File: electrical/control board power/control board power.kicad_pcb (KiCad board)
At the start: 2 copper layers, 147.3 x 147.3 mm, 69 parts, among them J1 Conn_01x02, J10 48V_from_conversion, J17 Switch_B, J18 Switch_C, J19 Switch_D, J2 5V, J3 Barrel_Jack, J4 Switch_A, J5 Switch_Input, J6 Power_Connector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

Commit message: Found some parts
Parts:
- added C14: C_Small, Capacitor_SMD:C_0603_1608Metric_Pad1.05x0.95mm_HandSolder, F.Cu at (25.9, 53.9)
- added R11: 1m, footprints:FC4L64, F.Cu at (34.4, 53.4)
- added U4: INA240-INA240, Package_SO:TSSOP-8_4.4x3mm_P0.65mm, F.Cu at (28.2, 51.4)
- R16, R3: footprint Resistor_SMD:R_0603_1608Metric_Pad1.05x0.95mm_HandSolder -> Resistor_SMD:R_1206_3216Metric_Pad1.42x1.75mm_HandSolder
- moved J1 23.1 mm to (81.2, 141.5)
- moved D1 7.40 mm to (45.5, 76.5)
- moved D3 7.40 mm to (45.5, 82.5)
- moved D8 7.40 mm to (45.5, 79.5)
- moved R1 7.40 mm to (50.5, 76.5)
- moved R16 7.40 mm to (50.5, 79.5)
- moved R3 7.40 mm to (50.5, 82.5)
- moved D2 7.40 mm to (45.5, 73.4)
- moved R2 7.40 mm to (50.5, 73.4)
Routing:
- net +24V: track 60.8 -> 91.7 mm
- net +5V: track 242.7 -> 250.5 mm
- net +48V: track 307.1 -> 313.8 mm
- net +3V3: track 59.6 -> 66.2 mm
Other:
- board text added: "These need to move"

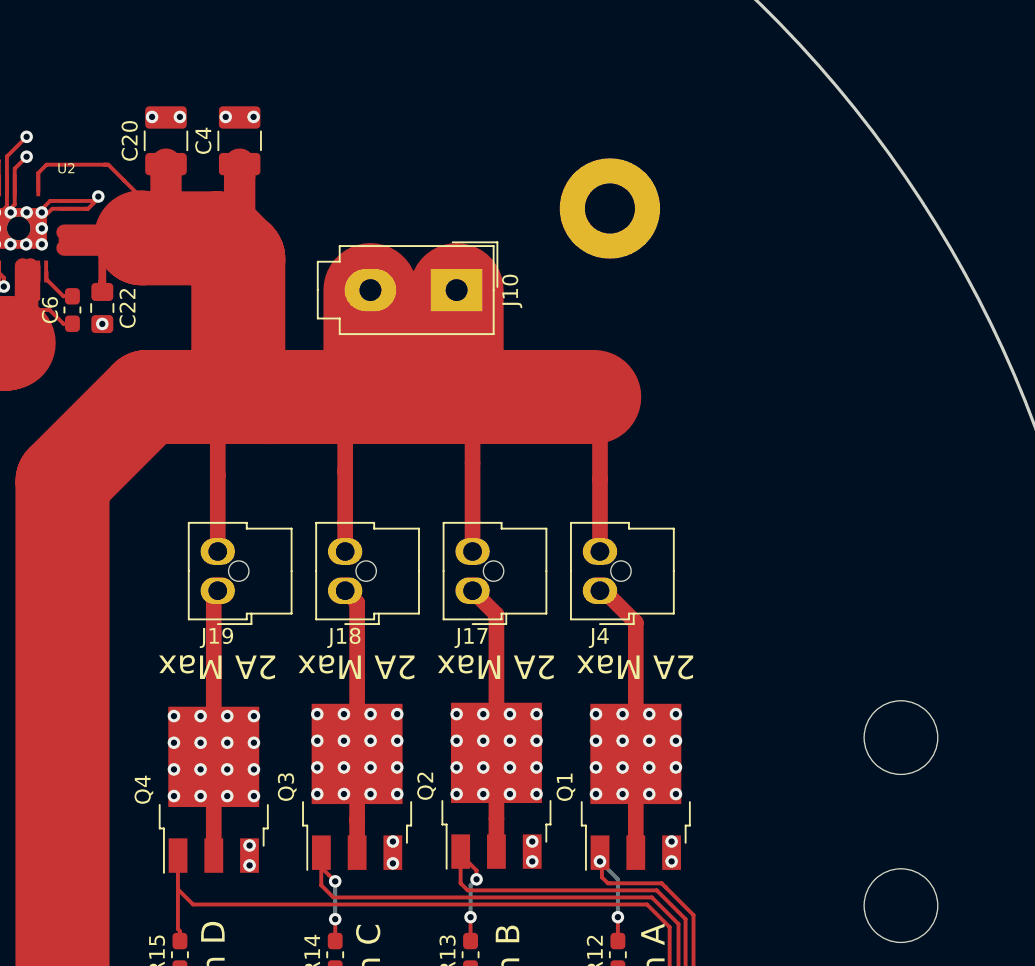
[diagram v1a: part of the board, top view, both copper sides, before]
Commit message: Making the low side switches beefier
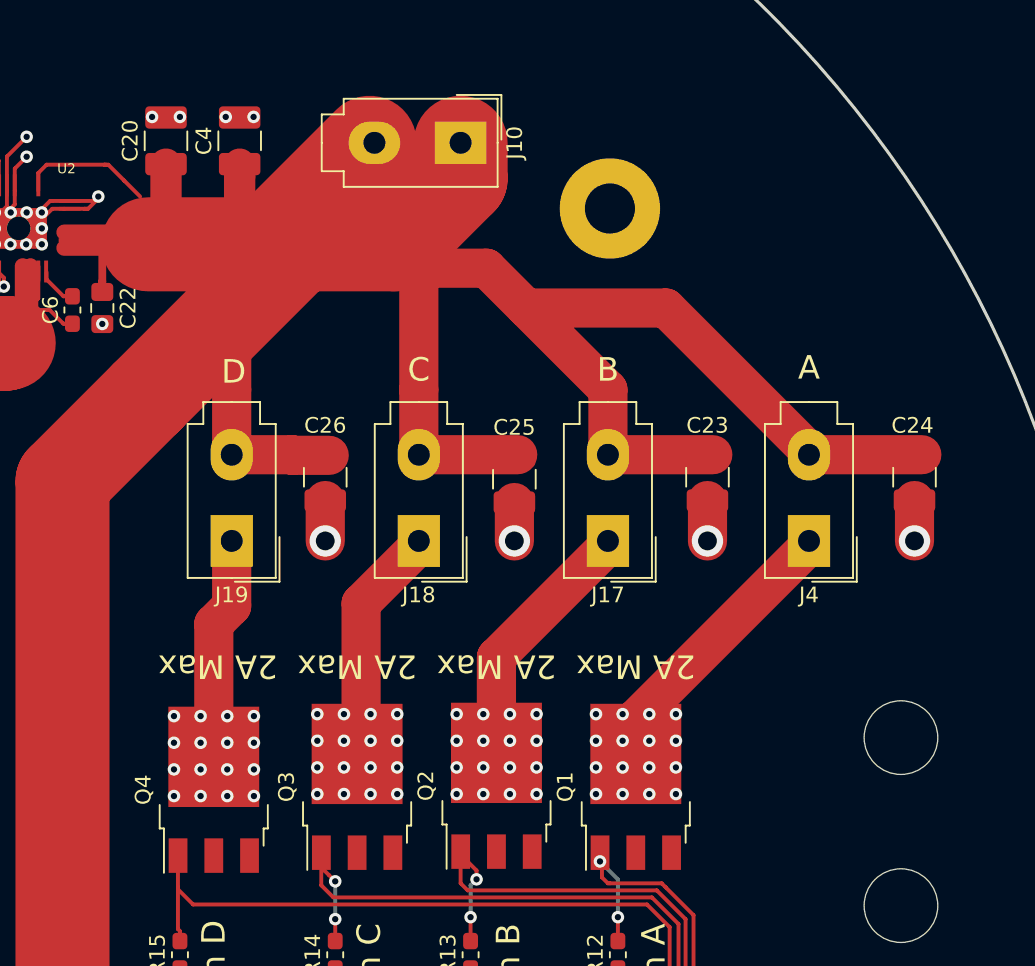
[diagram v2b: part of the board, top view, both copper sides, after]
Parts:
- added C23: 10uF, Capacitor_SMD:C_1210_3225Metric_Pad1.42x2.65mm_HandSolder, F.Cu at (149.7, 79.9)
- added C24: 10uF, Capacitor_SMD:C_1210_3225Metric_Pad1.42x2.65mm_HandSolder, F.Cu at (162.9, 79.9)
- added C25: 10uF, Capacitor_SMD:C_1210_3225Metric_Pad1.42x2.65mm_HandSolder, F.Cu at (137.4, 80.0)
- added C26: 10uF, Capacitor_SMD:C_1210_3225Metric_Pad1.42x2.65mm_HandSolder, F.Cu at (125.3, 79.9)
- J17, J18, J19, J4: footprint footprints:Molex_Nano-Fit_105309-xx02_1x02_P2.50mm_Vertical_Oval_Pads -> Connector_Molex:Molex_Mini-Fit_Jr_5566-02A_2x01_P4.20mm_Vertical
- moved J4 13.7 mm to (156.2, 83.9)
- moved J10 9.40 mm to (134.0, 58.5)
- moved J17 9.20 mm to (143.4, 83.9)
- moved J18 5.67 mm to (131.3, 83.9)
- moved J19 3.30 mm to (119.4, 83.9)
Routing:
- net +48V: track 313.8 -> 352.8 mm
- net GND: track 47.6 -> 57.8 mm, vias 85 -> 81
- net Net-(J4-Pad1): track 16.3 -> 18.3 mm
- net Net-(J19-Pad1): track 15.7 -> 14.3 mm
- net Net-(J17-Pad1): track 15.2 -> 15.9 mm
- net Net-(J18-Pad1): track 15.3 -> 14.7 mm
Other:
- board text added: "A"
- board text added: "B"
- board text added: "C"
- board text added: "D"
- board text removed: "These need to move"

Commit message: stuff
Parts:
- added D10: D_Small, Diode_SMD:D_SMC_Handsoldering, F.Cu at (196.8, 111.0)
- added D11: D_Small, Diode_SMD:D_SMC_Handsoldering, F.Cu at (210.6, 104.2)
- added D12: D_Small, Diode_SMD:D_SMC_Handsoldering, F.Cu at (210.6, 111.0)
- added D9: D_Small, Diode_SMD:D_SMC_Handsoldering, F.Cu at (203.7, 83.9)
- Q1, Q2, Q3, Q4: footprint Package_TO_SOT_SMD:TO-252-3_TabPin2 -> footprints:TO-252-3_2_Pin
- moved J1 7.90 mm to (75.6, 135.9)
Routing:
- net GND: track 57.8 -> 130.6 mm, vias 81 -> 84
- net +24V: track 91.7 -> 89.7 mm
- net +48V: track 352.8 -> 354.5 mm

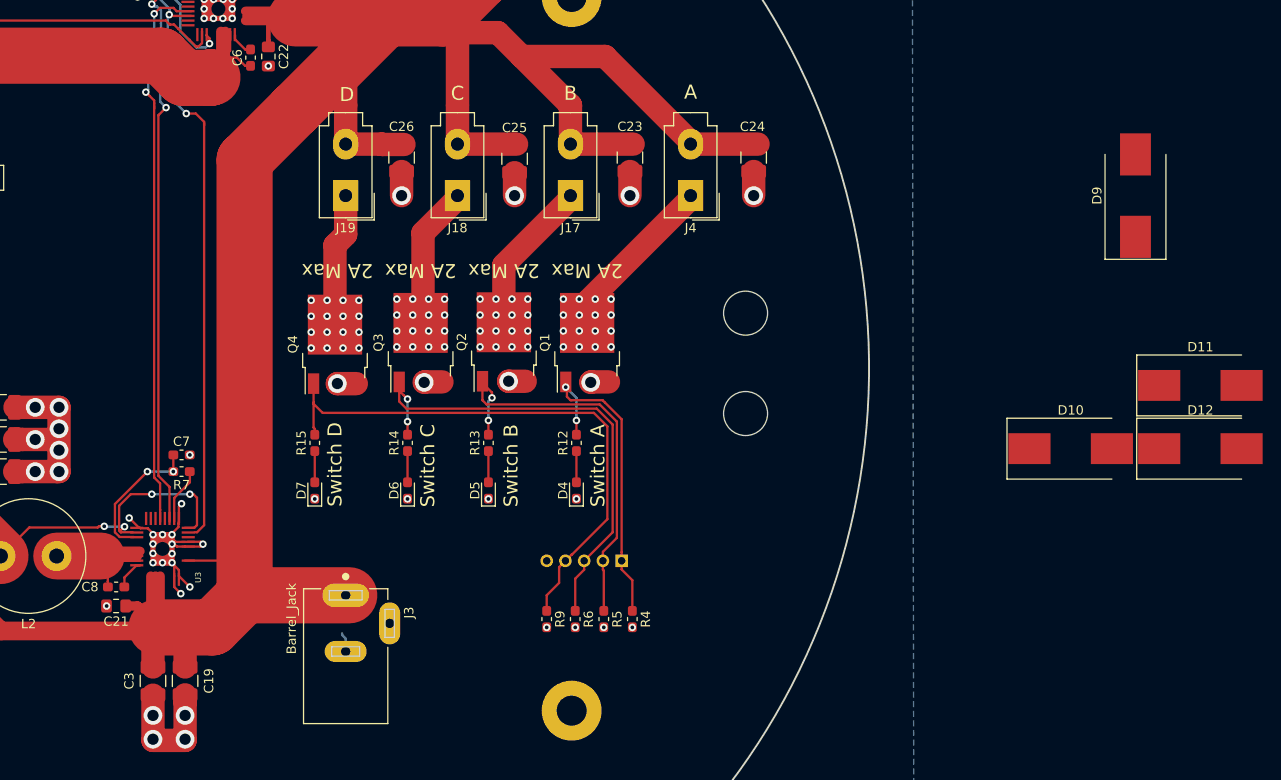
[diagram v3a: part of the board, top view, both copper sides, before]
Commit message: Added flyback diodes on low side switches
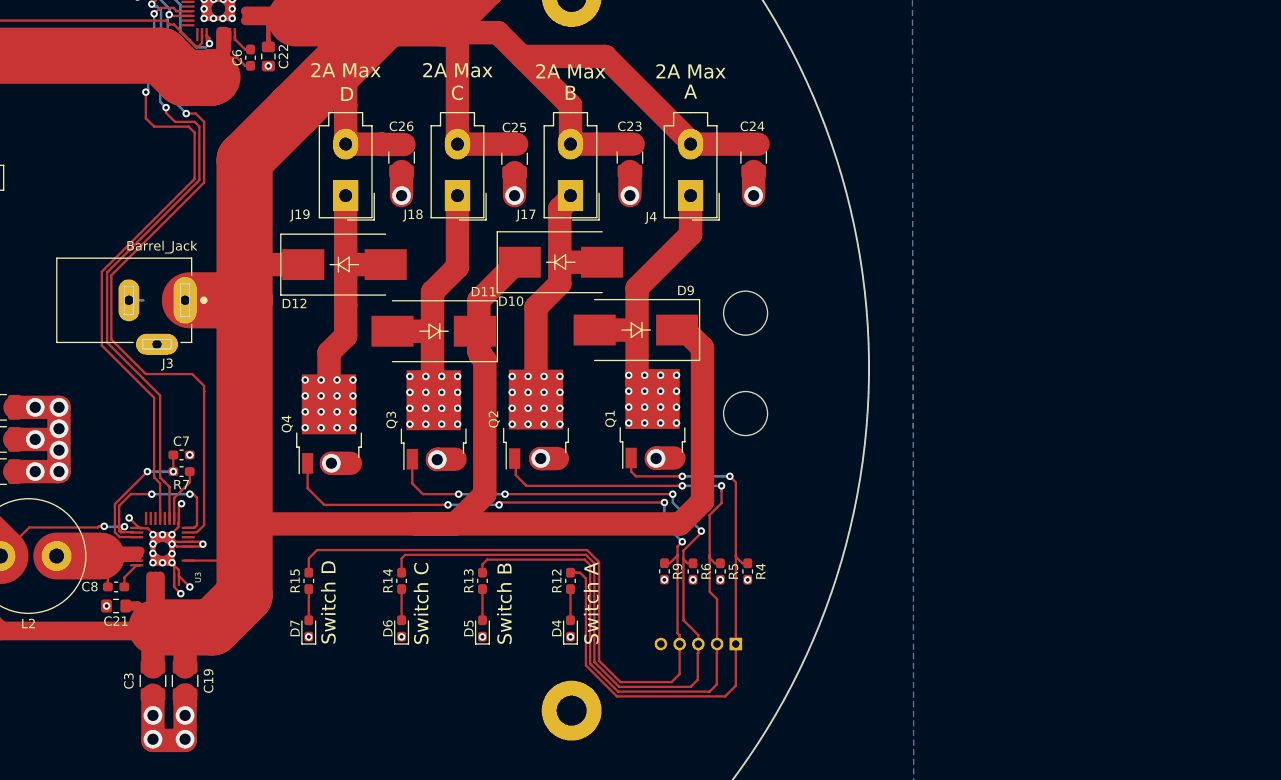
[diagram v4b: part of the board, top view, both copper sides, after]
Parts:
- D10, D11, D12, D9: footprint Diode_SMD:D_SMC_Handsoldering -> footprints:D_SMC_Handsoldering_Diode_Mark
- moved D12 93.5 mm to (119.3, 91.3)
- moved D11 82.1 mm to (128.8, 98.4), turned to 180 degrees
- moved D10 57.9 mm to (142.4, 91.1)
- moved D9 55.2 mm to (150.4, 98.3), turned to 180 degrees
- moved J3 35.9 mm to (102.2, 95.1), turned to 180 degrees
- moved J5 15.1 mm to (161.0, 131.8)
- moved D4 14.7 mm to (143.4, 130.2)
- moved D5 14.7 mm to (134.0, 130.2)
- moved D6 14.7 mm to (125.3, 130.2)
- moved D7 14.7 mm to (115.4, 130.2)
- moved R12 14.7 mm to (143.4, 125.1)
- moved R13 14.7 mm to (134.0, 125.1)
- moved R14 14.7 mm to (125.3, 125.1)
- moved R15 14.7 mm to (115.4, 125.1)
- moved R9 13.6 mm to (153.4, 124.1)
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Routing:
- net +48V: track 354.5 -> 459.3 mm
- net /SWITCH_D: track 60.5 -> 116.8 mm, vias 0 -> 4
- net /SWITCH_C: track 52.6 -> 100.0 mm, vias 2 -> 4
- net /SWITCH_B: track 44.0 -> 86.8 mm
- net /SWITCH_A: track 35.0 -> 64.9 mm
- net Net-(D12-Pad2): track 14.3 -> 27.1 mm
- net Net-(D11-Pad2): track 14.7 -> 26.4 mm
- net Net-(D10-Pad2): track 15.9 -> 27.5 mm
- net Net-(C10-Pad2): track 72.6 -> 83.6 mm
- net Net-(D9-Pad2): track 18.3 -> 28.6 mm
- net Net-(U2-Pad15): track 60.0 -> 69.8 mm
- net Net-(U2-Pad12): track 61.4 -> 70.1 mm
- net GND: track 130.6 -> 130.1 mm

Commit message: Moved indicator leds
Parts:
- moved D2 87.0 mm to (70.4, 156.7), turned to 180 degrees
- moved R2 84.6 mm to (65.3, 156.7), turned to 180 degrees
- moved D1 81.1 mm to (70.4, 153.7), turned to 180 degrees
- moved R1 78.6 mm to (65.3, 153.7), turned to 180 degrees
- moved D8 75.4 mm to (70.4, 150.6), turned to 180 degrees
- moved R16 72.6 mm to (65.3, 150.6), turned to 0 degrees
- moved D3 69.6 mm to (70.4, 147.6), turned to 180 degrees
- moved R3 66.7 mm to (65.3, 147.6), turned to 0 degrees
- moved J3 58.5 mm to (127.9, 42.5)
- moved G*** 4.51 mm to (102.9, 159.5)
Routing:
- net +3V3: track 66.2 -> 96.1 mm
- net +48V: track 459.3 -> 474.1 mm, vias 1 -> 0
- net Net-(C10-Pad2): track 83.6 -> 72.4 mm
- net +5V: track 250.5 -> 258.0 mm, vias 6 -> 4
- net Net-(U2-Pad12): track 70.1 -> 65.5 mm
- net Net-(U2-Pad15): track 69.8 -> 65.3 mm
- net GND: track 130.1 -> 131.4 mm
- net +24V: track 89.7 -> 88.5 mm, vias 4 -> 2
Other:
- board text added: "24V In"
- board text added: "Did you unplug the 48V?"
- board text added: "GND"
- board text added: "MATE Control Power Board 2019 Designed by Timmy Beuchel Rev. 1"
- board text added: "Power Out"
- board text removed: "MATE Control Power Board 2019 Rev. 1"
